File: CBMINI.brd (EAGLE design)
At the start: 100 x 60 mm, 59 parts, among them IC1 ATMEGA32U4NT-TQFP, IC2 MCP2515, IC3 MCP2551, J1 USB-B-PTH, X1 INPUT, X2 OUTPUT

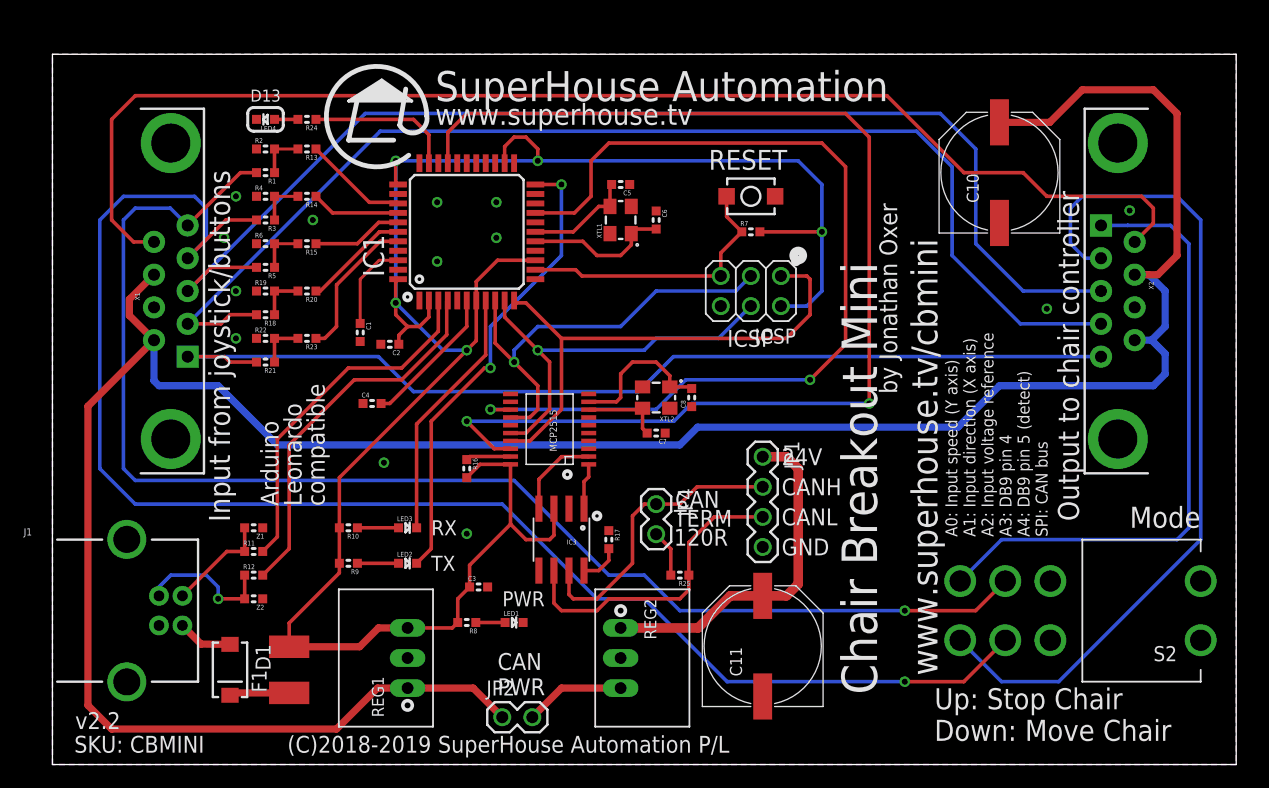
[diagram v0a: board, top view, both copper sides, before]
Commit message: Isolation diodes between CAN and chair power, and switched parts to SuperHouse libraries for v2.3 release
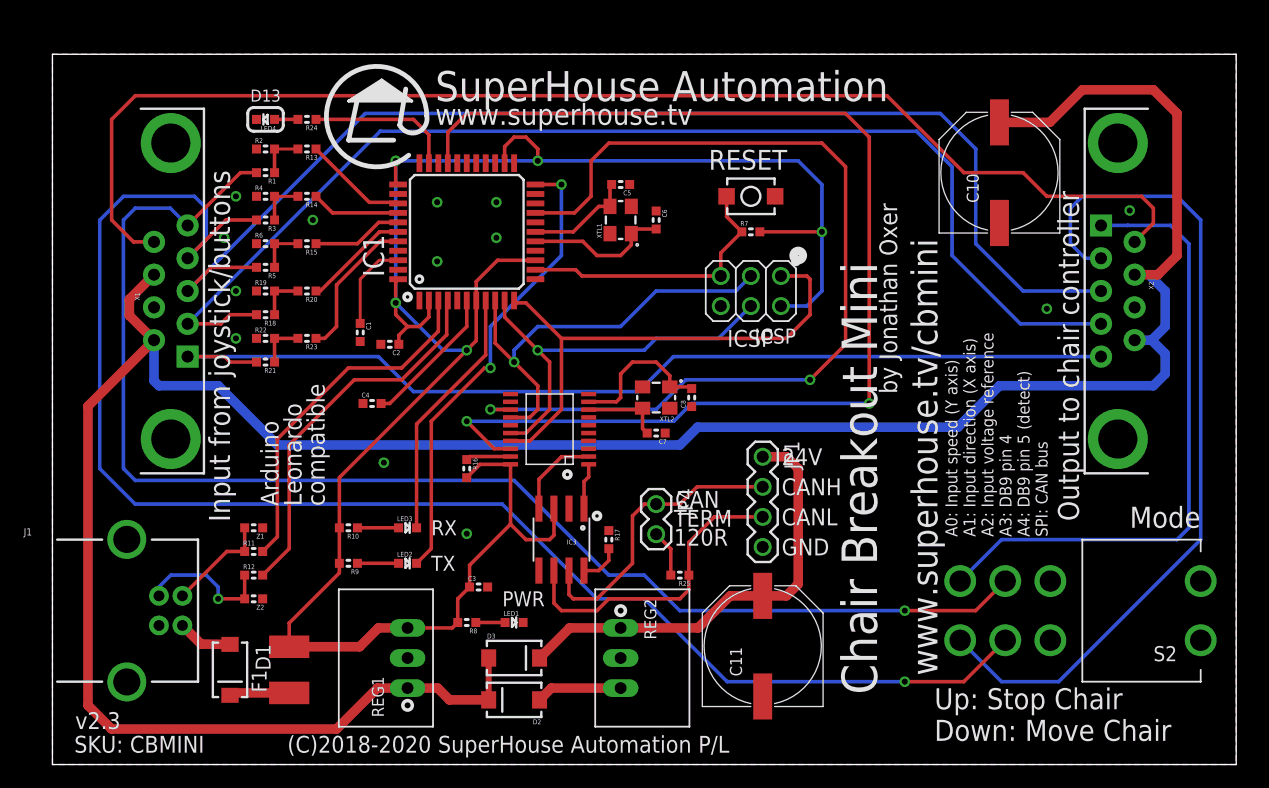
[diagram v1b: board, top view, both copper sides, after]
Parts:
- removed JP2: PWR, SuperHouse-Connectors:1X02-P
- added D2, D3: SS56, SuperHouse-DiscreteSemi:SMA-DIODE
- D1: value 1N4004 -> SS56
- S2: device freetronics-jon:7201SD9AV2BE -> SuperHouse-Switches:7201SD9AV2BE
- X1: device SparkFun-Connectors:DB9_MALE -> SuperHouse-Connectors:DB9-PCB-PLUG
- X2: device SparkFun-Connectors:DB9 -> SuperHouse-Connectors:DB9-PCB-SOCKET
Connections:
- net 12V: now also D2.A; no longer JP2.2
- net 24V: now also D3.C
- net VREF: now also D2.C, D3.A; no longer JP2.1
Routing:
- net 24V: track 29.7 -> 37.6 mm
- net VREF: track 218.0 -> 219.8 mm
- net 12V: track 8.48 -> 7.26 mm
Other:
- board text added: "(C)2018-2020 SuperHouse Automation P/L"
- board text added: "v2.3"
- board text removed: "(C)2018-2019 SuperHouse Automation P/L"
- board text removed: "CAN PWR"
- board text removed: "v2.2"
